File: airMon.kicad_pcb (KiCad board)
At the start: 2 copper layers, 64.8 x 99.7 mm, 126 parts, among them J1 JTAG, J10 I2C_2_2, J11 I2C_2_3_Buffer, J12 I2C_2_4_Buffer, J13 GPS, J14 A3, J15 A4, J16 Rain, J17 GPIO, J18 Wind, J19 USB_B_Micro, J2 PMS7003, J20 Power, J3 PMSx003, J4 SDS011, J5 Conn_01x05, J6 SW, J7 I2C_1_1, J8 I2C_1_2, J9 I2C_2_1, Q1 2N7002, Q2 AO3401A, Q3 SS8050, Q4 SS8050, Q5 2N7002, Q6 DMP6023LE-13, Q7 2N7002, Q8 DMP6023LE-13, Q9 DMP6023LE-13, SW1 RESET, SW2 Boot, U1 ESP32-WROOM-32, U2 P82B715, U3 L70/L76/MAX-M8C/MAX-M8Q/MAX-8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, U4 PCA9536D, U5 CH340C, U6 LMR14010ADDCR, U7 LMR14010ADDCR

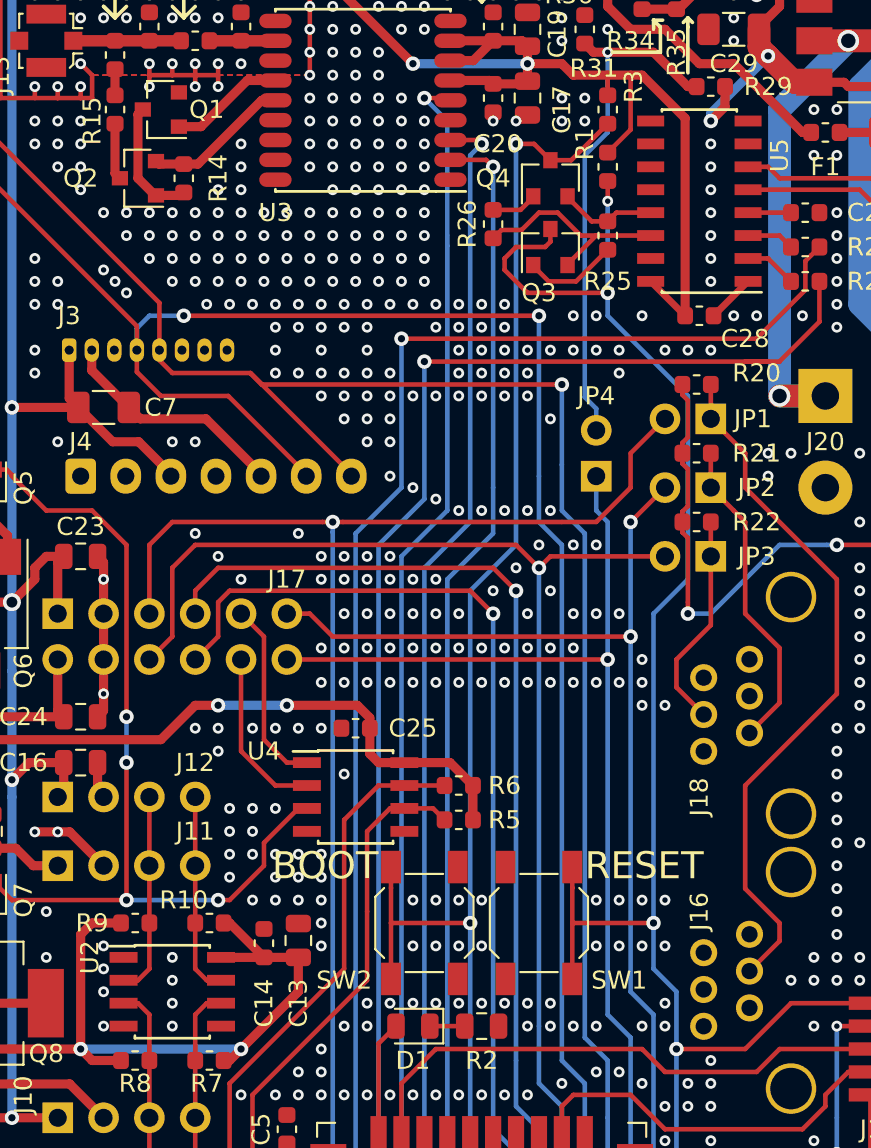
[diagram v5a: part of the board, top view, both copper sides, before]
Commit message: Start of v0.2 Updated footprints
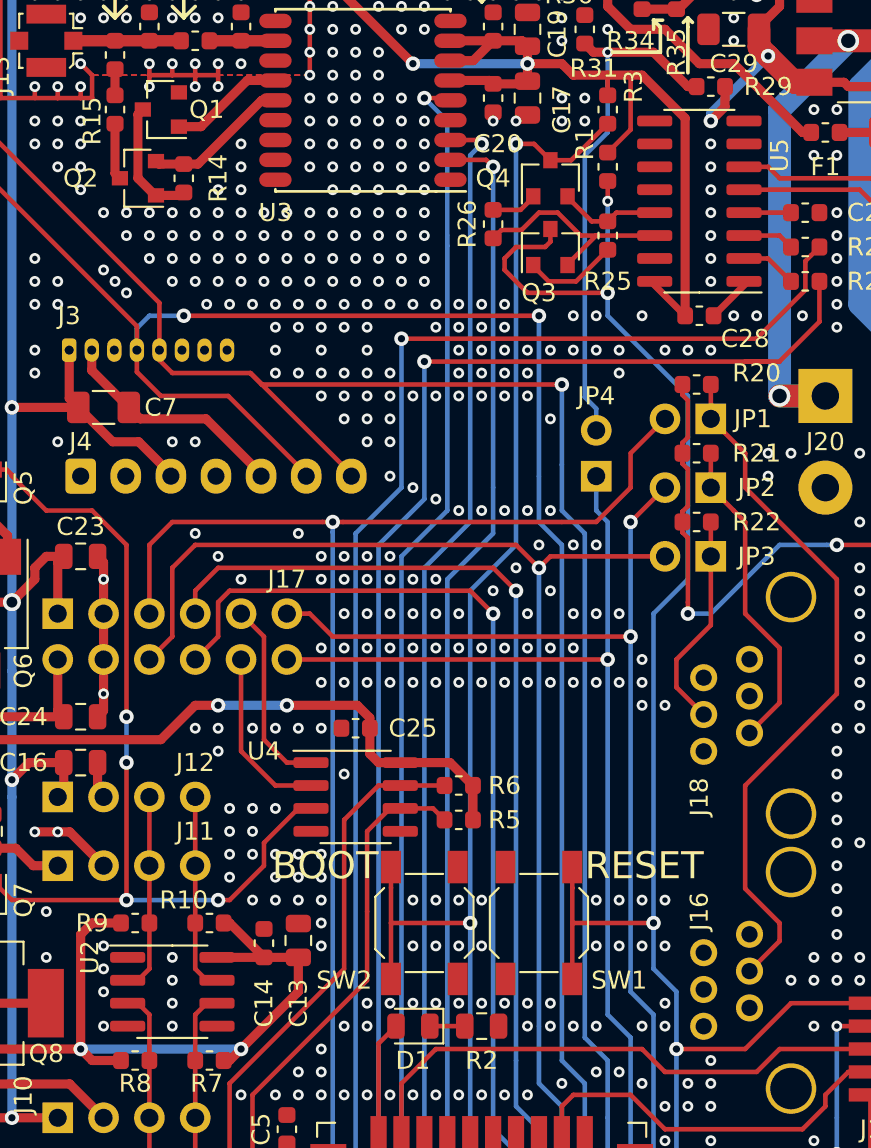
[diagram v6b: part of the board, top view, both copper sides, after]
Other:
- board text added: "v0.2"
- board text removed: "v0.1"
